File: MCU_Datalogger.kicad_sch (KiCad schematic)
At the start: 25 parts, among them U1 24LC1025, U2 24LC1025, U3 DS1337S_, U4 ATMEGA328P-AU, Y1 32.768 KHz, Y2 16 MHz

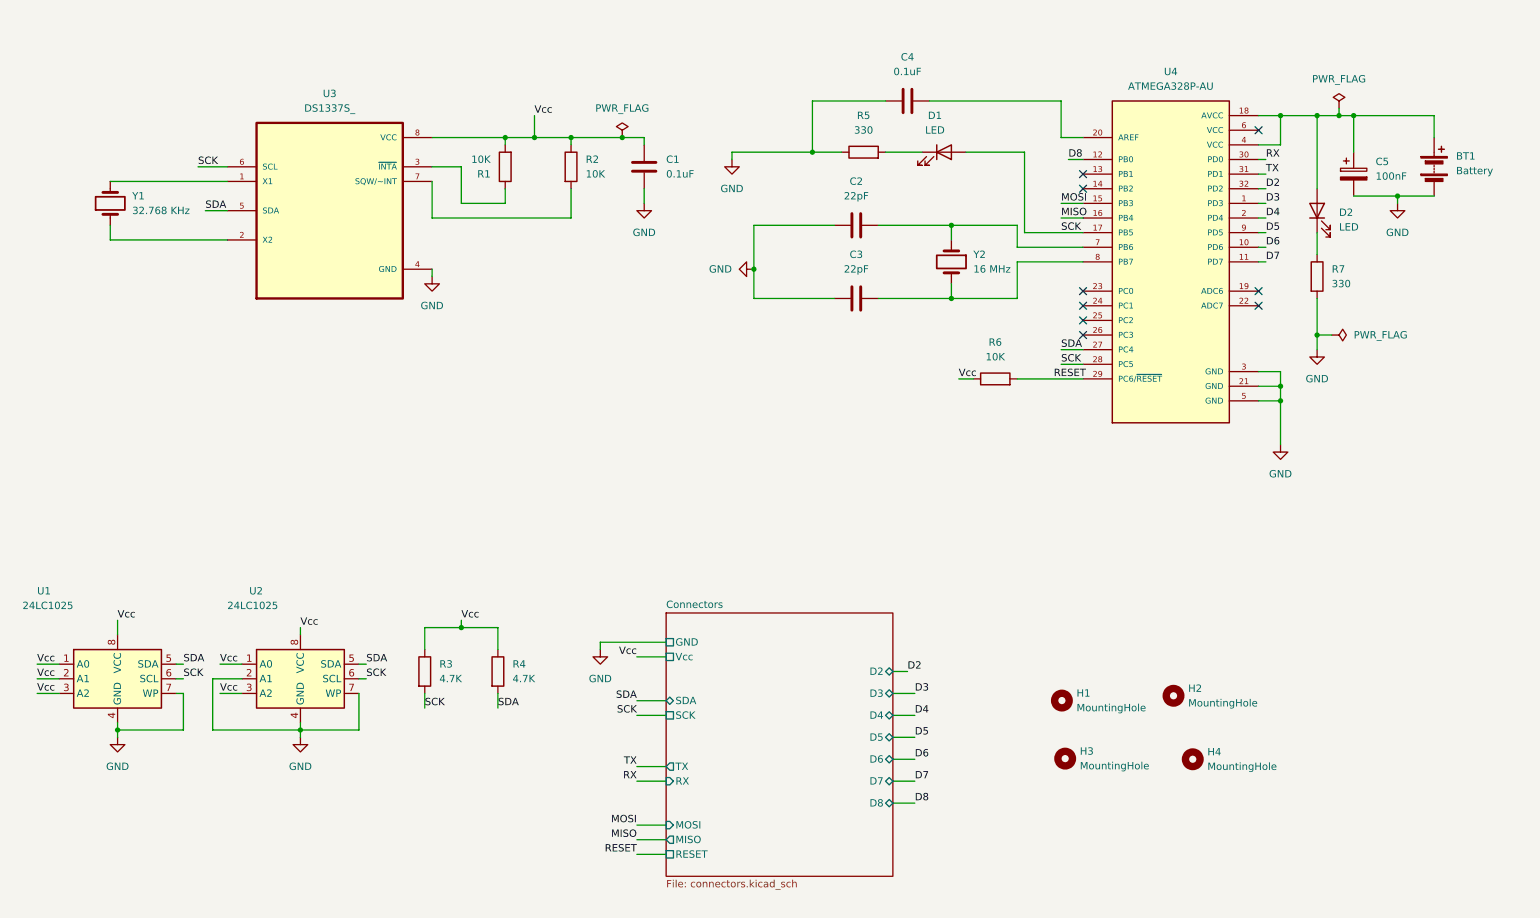
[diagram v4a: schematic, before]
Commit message: Fixed various errors and made the PCB more redeable
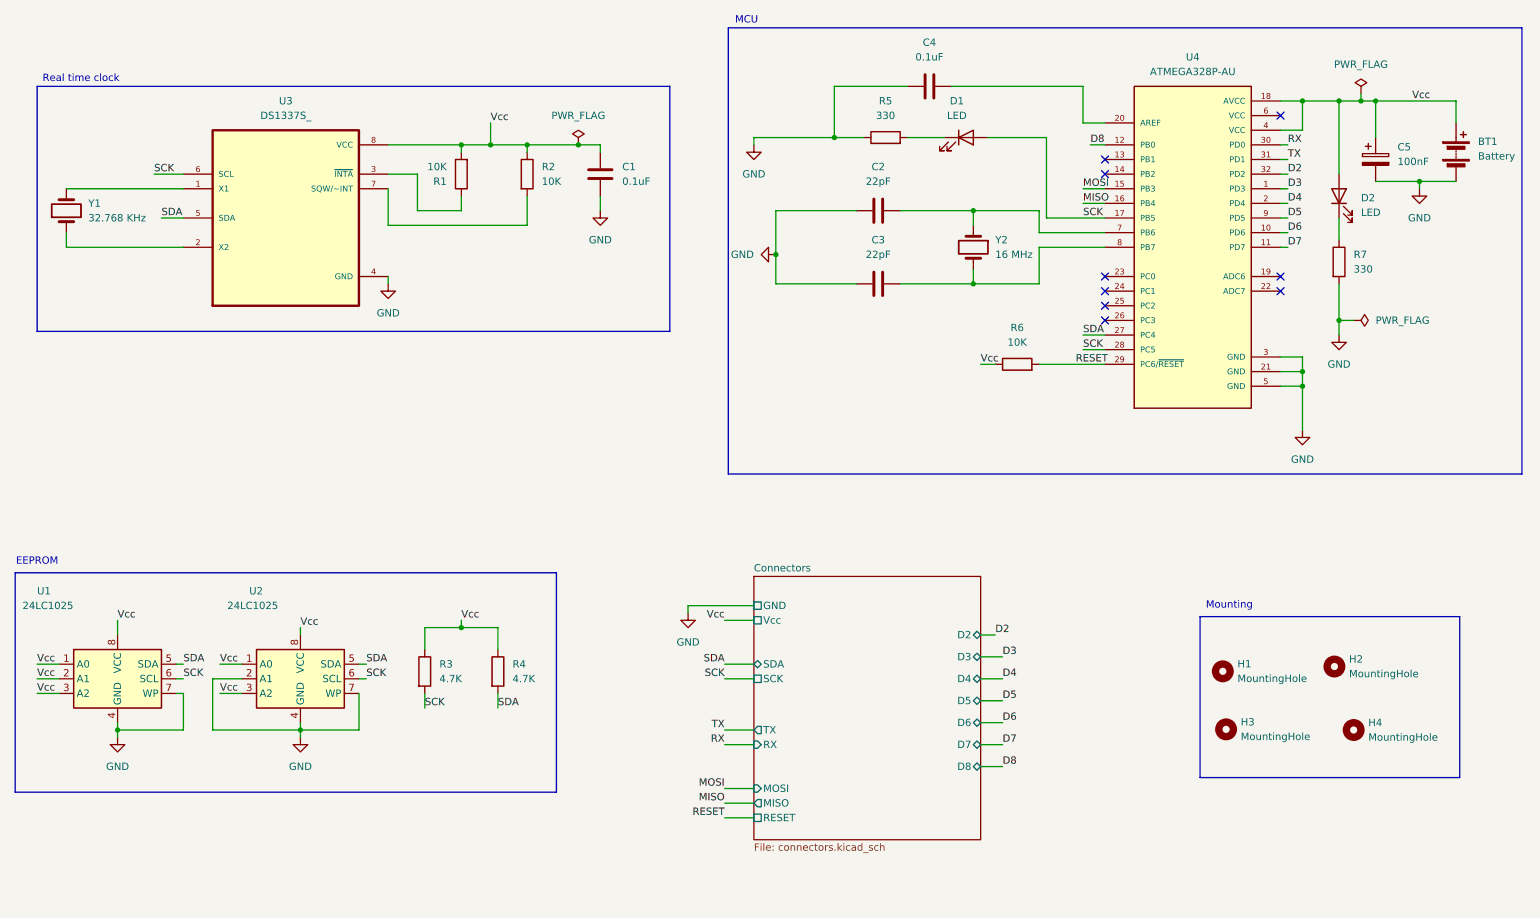
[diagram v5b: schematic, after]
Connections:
- net Vcc: now also BT1.1 (+), C5.1, D2.2 (A), U4.18 (AVCC), U4.4 (VCC)
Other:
- note added: "EEPROM"
- note added: "MCU"
- note added: "Mounting"
- note added: "Real time clock"
- moved on the sheet: BT1, C1, C2, C3, C4, C5, D1, D2, H1, H2, H3, H4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

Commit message: Fixed 2 bugs in the Schematics diagram
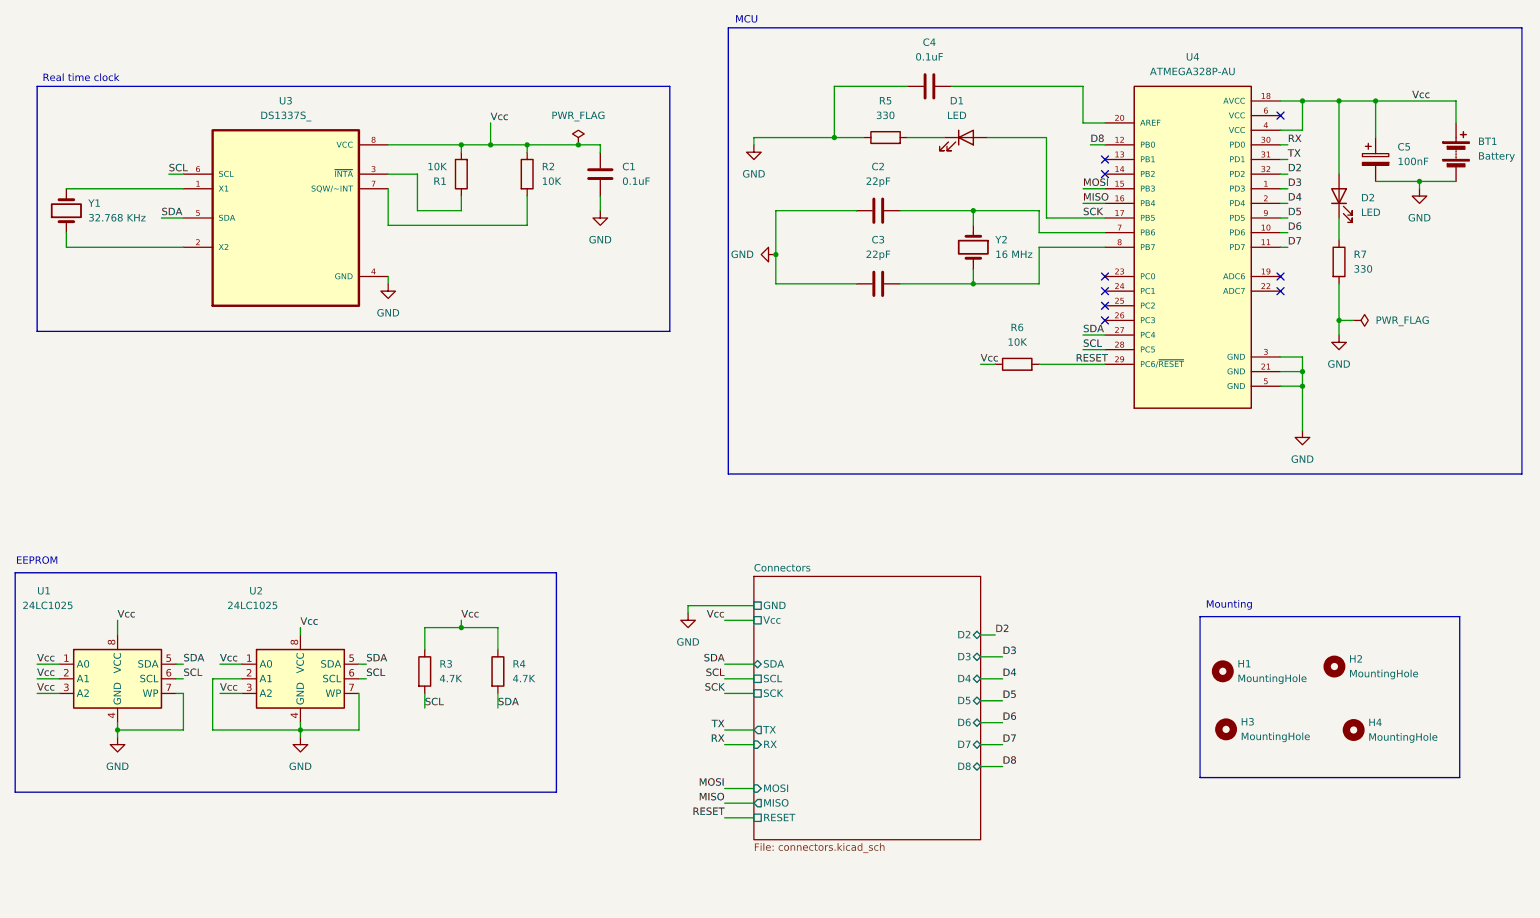
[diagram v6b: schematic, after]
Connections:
- net SCK: no longer R3.2, U1.6 (SCL), U2.6 (SCL), U3.6 (SCL), U4.28 (PC5)
- new net SCL: R3.2, U1.6 (SCL), U2.6 (SCL), U3.6 (SCL), U4.28 (PC5)
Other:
- sheet Connectors ports: added SCL; removed none
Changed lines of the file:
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@@
 	)
 	(junction
-		(at 255.27 27.94)
-		(diameter 0)
-		(color 0 0 0 0)
-	)
-	(junction
 		(at 251.46 66.04)
 		(diameter 0)
@@
 	(wire
 		(pts
-			(xy 45.72 40.64) (xy 50.8 40.64)
+			(xy 48.26 40.64) (xy 50.8 40.64)
 		)
 		(stroke
@@
 	(wire
 		(pts
-			(xy 251.46 27.94) (xy 255.27 27.94)
-		)
-		(stroke
-			(width 0)
-			(type default)
-		)
-	)
-	(wire
-		(pts
 			(xy 92.71 133.35) (xy 92.71 130.81)
 		)
@@
 	(wire
 		(pts
-			(xy 255.27 26.67) (xy 255.27 27.94)
-		)
-		(stroke
-			(width 0)
-			(type default)
-		)
-	)
-	(wire
-		(pts
 			(xy 189.23 120.65) (xy 191.77 120.65)
 		)
@@
 	(wire
 		(pts
+			(xy 144.78 130.81) (xy 149.86 130.81)
+		)
+		(stroke
+			(width 0)
+			(type default)
+		)
+	)
+	(wire
+		(pts
 			(xy 55.88 137.16) (xy 55.88 128.27)
 		)
@@
 	(wire
 		(pts
-			(xy 255.27 27.94) (xy 257.81 27.94)
+			(xy 251.46 27.94) (xy 257.81 27.94)
 		)
 		(stroke
@@
 		)
 	)
-	(label "D7"
-		(at 242.57 53.34 0)
+	(label "SCK"
+		(at 144.78 130.81 180)
 		(effects
 			(font
 				(size 1.27 1.27)
 			)
-			(justify left bottom)
+			(justify right bottom)
 		)
 	)
-	(label "SDA"
-		(at 46.99 48.26 0)
+	(label "D7"
+		(at 242.57 53.34 0)
 		(effects
 			(font
@@
 		)
 	)
-	(label "D3"
-		(at 193.04 124.46 0)
+	(label "SDA"
+		(at 46.99 48.26 0)
 		(effects
 			(font
@@
 		)
 	)
-	(label "SCK"
-		(at 45.72 40.64 0)
+	(label "D3"
+		(at 193.04 124.46 0)
 		(effects
 			(font
@@
 		)
 	)
+	(label "SCL"
+		(at 50.8 128.27 0)
+		(effects
+			(font
+				(size 1.27 1.27)
+			)
+			(justify left bottom)
+		)
+	)
 	(label "SDA"
 		(at 50.8 125.73 0)
@@
 		)
 	)
-	(label "SCK"
-		(at 82.55 128.27 0)
-		(effects
-			(font
-				(size 1.27 1.27)
-			)
-			(justify left bottom)
-		)
-	)
 	(label "Vcc"
 		(at 57.15 130.81 0)
@@
 		)
 	)
-	(label "SCK"
-		(at 50.8 128.27 0)
-		(effects
-			(font
-				(size 1.27 1.27)
-			)
-			(justify left bottom)
-		)
-	)
 	(label "Vcc"
 		(at 25.4 130.81 0)
@@
 		)
 	)
-	(label "SCK"
+	(label "SCL"
 		(at 207.01 71.12 0)
 		(effects
@@
 		)
 	)
+	(label "SCL"
+		(at 92.71 133.35 0)
+		(effects
+			(font
+				(size 1.27 1.27)
+			)
+			(justify left bottom)
+		)
+	)
 	(label "Vcc"
 		(at 25.4 125.73 0)
@@
 		)
 	)
+	(label "SCL"
+		(at 82.55 128.27 0)
+		(effects
+			(font
+				(size 1.27 1.27)
+			)
+			(justify left bottom)
+		)
+	)
 	(label "Vcc"
 		(at 189.23 73.66 0)
@@
 		)
 	)
-	(label "SCK"
+	(label "SCL"
+		(at 48.26 40.64 0)
+		(effects
+			(font
+				(size 1.27 1.27)
+			)
+			(justify left bottom)
+		)
+	)
+	(label "SCL"
 		(at 144.78 128.27 180)
 		(effects
@@
 		)
 	)
-	(label "SCK"
-		(at 92.71 133.35 0)
-		(effects
-			(font
-				(size 1.27 1.27)
-			)
-			(justify left bottom)
-		)
-	)
 	(symbol
 		(lib_id "Device:R")
@@
 	)
 	(symbol
-		(lib_id "power:PWR_FLAG")
-		(at 255.27 26.67 0)
-		(unit 1)
-		(exclude_from_sim no)
-		(in_bom yes)
-		(on_board yes)
-		(dnp no)
-		(fields_autoplaced yes)
-		(property "Reference" "#FLG01"
-			(at 255.27 24.765 0)
-			(effects
-				(font
-					(size 1.27 1.27)
-				)
-				(hide yes)
-			)
-		)
-		(property "Value" "PWR_FLAG"
-			(at 255.27 21.59 0)
-			(effects
-				(font
-					(size 1.27 1.27)
-				)
-			)
-		)
-		(property "Footprint" ""
-			(at 255.27 26.67 0)
-			(effects
-				(font
-					(size 1.27 1.27)
-				)
-				(hide yes)
-			)
-		)
-		(property "Datasheet" "~"
-			(at 255.27 26.67 0)
-			(effects
-				(font
-					(size 1.27 1.27)
-				)
-				(hide yes)
-			)
-		)
-		(property "Description" "Special symbol for telling ERC where power comes from"
-			(at 255.27 26.67 0)
-			(effects
-				(font
-					(size 1.27 1.27)
-				)
-				(hide yes)
-			)
-		)
-		(pin "1"
-		)
-		(instances
-			(project ""
-				(path "/5b67eaba-932b-46d3-9741-3df920aa422f"
-					(reference "#FLG01")
-					(unit 1)
-				)
-			)
-		)
-	)
-	(symbol
 		(lib_id "Device:Crystal")
 		(at 187.96 53.34 270)
@@
 			)
 		)
-		(pin "SCK" passive
-			(at 149.86 128.27 180)
+		(pin "SDA" bidirectional
+			(at 149.86 125.73 180)
 			(effects
 				(font
@@
 			)
 		)
-		(pin "SDA" bidirectional
-			(at 149.86 125.73 180)
+		(pin "TX" output
+			(at 149.86 137.16 180)
 			(effects
 				(font
@@
 			)
 		)
-		(pin "TX" output
-			(at 149.86 137.16 180)
+		(pin "Vcc" passive
+			(at 149.86 118.11 180)
 			(effects
 				(font
@@
 			)
 		)
-		(pin "Vcc" passive
-			(at 149.86 118.11 180)
+		(pin "SCL" passive
+			(at 149.86 128.27 180)
+			(effects
+				(font
+					(size 1.27 1.27)
+				)
+				(justify left)
+			)
+		)
+		(pin "SCK" passive
+			(at 149.86 130.81 180)
 			(effects
 				(font
